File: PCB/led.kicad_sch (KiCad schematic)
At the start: 52 parts, among them U1 TLC59461PWP, U2 TLC59461PWP, U3 TLC59461PWP

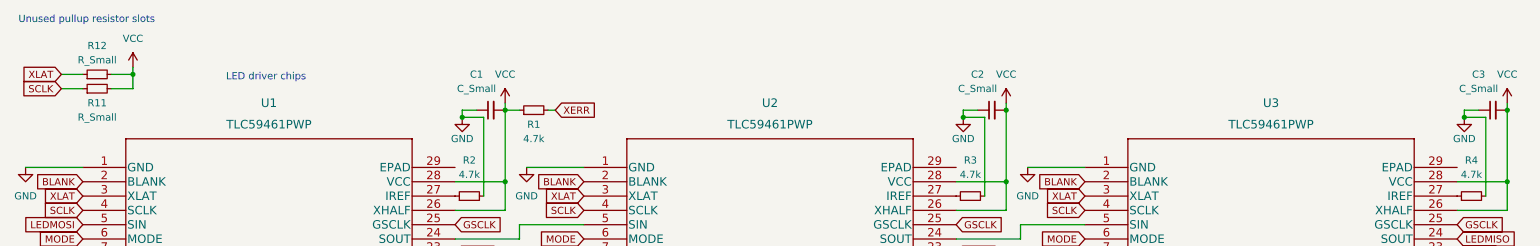
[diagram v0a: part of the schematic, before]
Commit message: Migrate to kicad7 and component updates
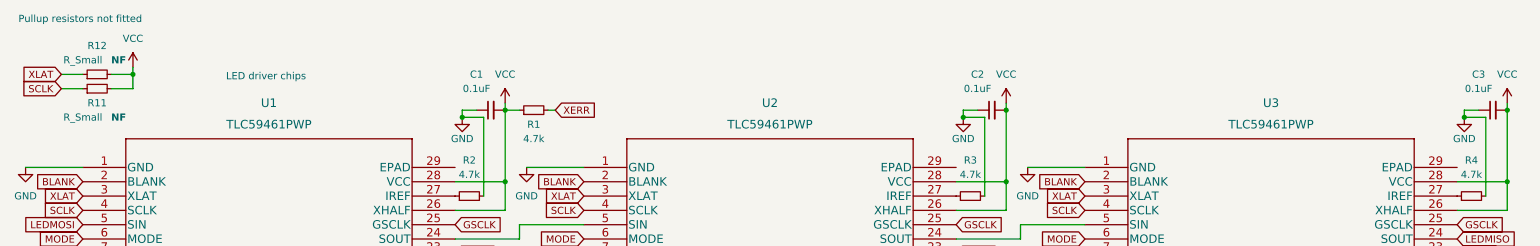
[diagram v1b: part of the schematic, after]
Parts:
- C1, C2, C3: value C_Small -> 0.1uF
- R11, R12: NotFitted (none) -> NF
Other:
- note added: "Pullup resistors not fitted"
- note removed: "Unused pullup resistor slots"
